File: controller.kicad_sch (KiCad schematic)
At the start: 24 parts, among them U1 nRF52840, X1 32MHz, X2 32.768kHz

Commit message: Start routing antennna
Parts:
- AE1: footprint (none) -> RF_Antenna:Texas_SWRA117D_2.4GHz_Left
- L1: footprint Inductor_SMD:L_6.3x6.3_H3 -> Inductor_SMD:L_0603_1608Metric
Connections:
- net VDD: now also C10.1, C5.1, C7.1, C8.1, C9.1, U1.A22 (VDD), U1.AD14 (VDD), U1.AD23 (VDD), U1.B1 (VDD), U1.W1 (VDD)
- net VDD_HV renamed VDDH
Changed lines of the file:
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@@
   (junction (at 72.39 113.03) (diameter 0) (color 0 0 0 0)
   )
-  (junction (at 50.8 27.94) (diameter 0) (color 0 0 0 0)
-  )
   (junction (at 149.86 36.83) (diameter 0) (color 0 0 0 0)
   )
@@
   (junction (at 72.39 123.19) (diameter 0) (color 0 0 0 0)
   )
-  (junction (at 140.97 16.51) (diameter 0) (color 0 0 0 0)
-  )
   (junction (at 72.39 57.15) (diameter 0) (color 0 0 0 0)
   )
@@
     (stroke (width 0) (type default))
   )
-  (wire (pts (xy 140.97 15.24) (xy 140.97 16.51))
-    (stroke (width 0) (type default))
-  )
   (wire (pts (xy 59.69 45.72) (xy 59.69 46.99))
     (stroke (width 0) (type default))
@@
     (stroke (width 0) (type default))
   )
-  (wire (pts (xy 41.91 27.94) (xy 50.8 27.94))
-    (stroke (width 0) (type default))
-  )
   (wire (pts (xy 46.99 44.45) (xy 46.99 46.99))
     (stroke (width 0) (type default))
@@
   (wire (pts (xy 72.39 121.92) (xy 72.39 123.19))
     (stroke (width 0) (type default))
-  )
-  (label "VDD_HV" (at 140.97 15.24 0) (fields_autoplaced)
-    (effects (font (size 1.27 1.27)) (justify left bottom))
   )
   (global_label "SWC" (shape input) (at 78.74 163.83 180) (fields_autoplaced)
@@
     )
   )
+  (global_label "VDDH" (shape input) (at 140.97 16.51 0) (fields_autoplaced)
+    (effects (font (size 1.27 1.27)) (justify left))
+    (property "Intersheetrefs" "${INTERSHEET_REFS}" (at 148.9143 16.51 0)
+      (effects (font (size 1.27 1.27)) (justify left) hide)
+    )
+  )
   (global_label "ROW4" (shape input) (at 144.78 69.85 0) (fields_autoplaced)
     (effects (font (size 1.27 1.27)) (justify left))
@@
     )
   )
+  (global_label "VDD" (shape input) (at 50.8 27.94 180) (fields_autoplaced)
+    (effects (font (size 1.27 1.27)) (justify right))
+    (property "Intersheetrefs" "${INTERSHEET_REFS}" (at 44.1862 27.94 0)
+      (effects (font (size 1.27 1.27)) (justify right) hide)
+    )
+  )
   (global_label "ROW1" (shape input) (at 144.78 146.05 0) (fields_autoplaced)
     (effects (font (size 1.27 1.27)) (justify left))
@@
       (effects (font (size 1.27 1.27)))
     )
-    (property "Footprint" "" (at 25.4 72.39 0)
+    (property "Footprint" "RF_Antenna:Texas_SWRA117D_2.4GHz_Left" (at 25.4 72.39 0)
       (effects (font (size 1.27 1.27)) hide)
     )
@@
       (effects (font (size 1.27 1.27)))
     )
-    (property "Footprint" "Inductor_SMD:L_6.3x6.3_H3" (at 128.27 45.72 0)
-      (effects (font (size 1.27 1.27)) hide)
-    )
+    (property "Footprint" "Inductor_SMD:L_0603_1608Metric" (at 128.27 45.72 0)
+      (effects (font (size 1.27 1.27)) hide)
+    )

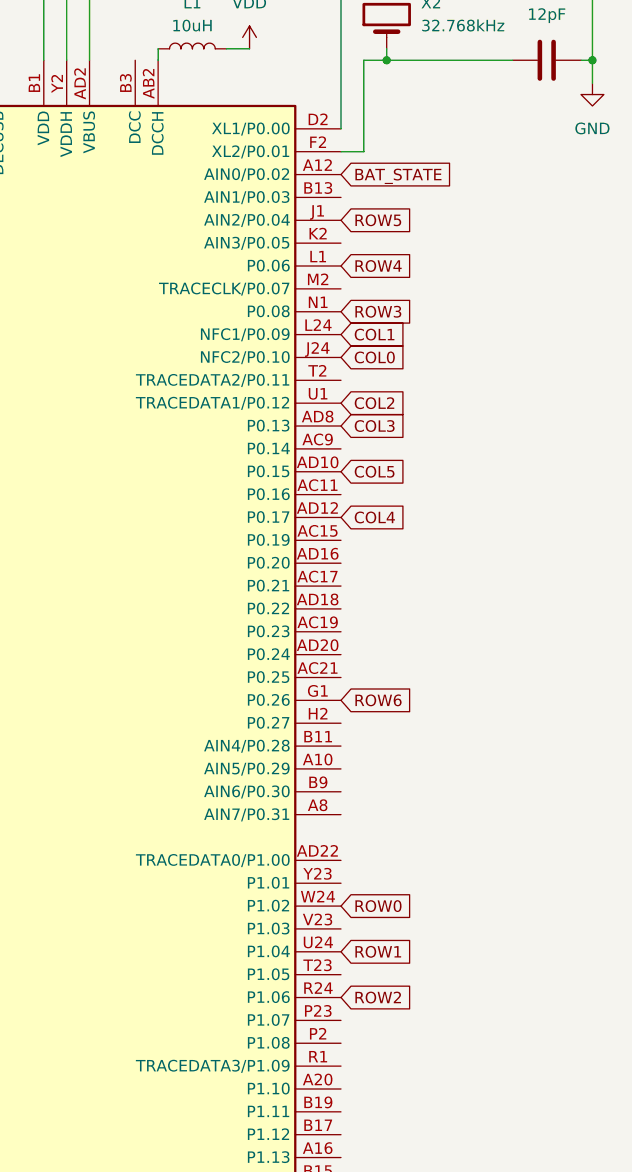
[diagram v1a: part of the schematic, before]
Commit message: Change board shape
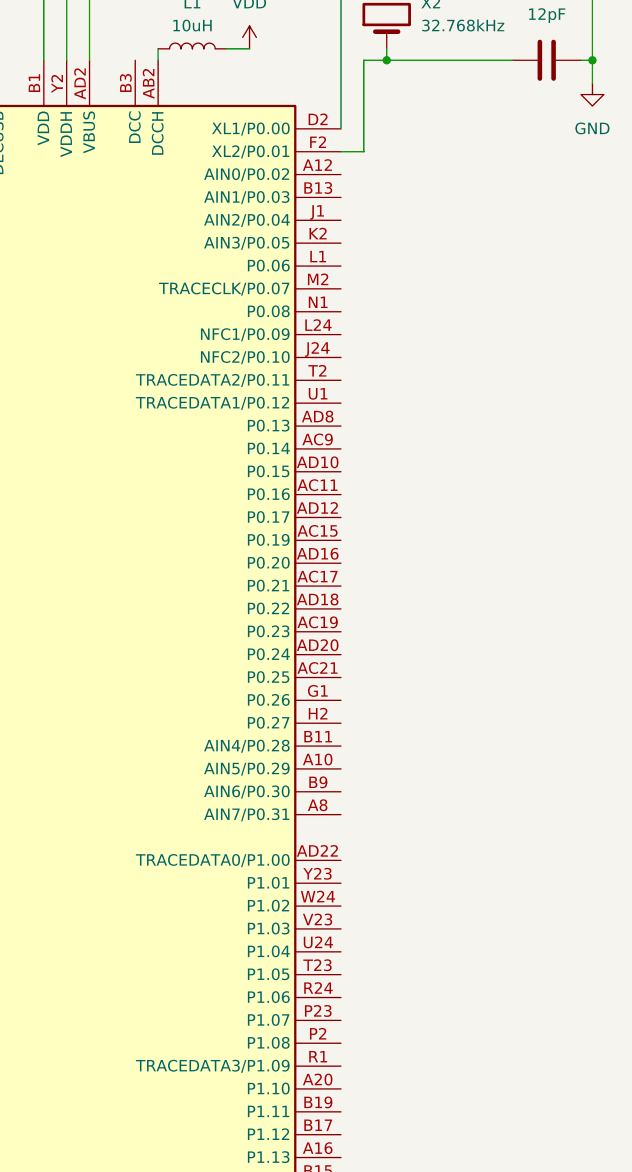
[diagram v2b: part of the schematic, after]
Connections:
- net BAT_STATE: no longer names the net of U1.A12 (AIN0/P0.02)
- net COL0: no longer names the net of U1.J24 (NFC2/P0.10)
- net COL1: no longer names the net of U1.L24 (NFC1/P0.09)
- net COL2: no longer names the net of U1.U1 (TRACEDATA1/P0.12)
- net COL3: no longer names the net of U1.AD8 (P0.13)
- net COL4: no longer names the net of U1.AD12 (P0.17)
- net COL5: no longer names the net of U1.AD10 (P0.15)
- net ROW0: no longer names the net of U1.W24 (P1.02)
- net ROW1: no longer names the net of U1.U24 (P1.04)
- net ROW2: no longer names the net of U1.R24 (P1.06)
- net ROW3: no longer names the net of U1.N1 (P0.08)
- net ROW4: no longer names the net of U1.L1 (P0.06)
- net ROW5: no longer names the net of U1.J1 (AIN2/P0.04)
- net ROW6: no longer names the net of U1.G1 (P0.26)
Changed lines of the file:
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@@
-    )
-  )
-  (global_label "ROW4" (shape input) (at 144.78 69.85 0) (fields_autoplaced)
-    (effects (font (size 1.27 1.27)) (justify left))
-    (property "Intersheetrefs" "${INTERSHEET_REFS}" (at 153.0266 69.85 0)
-      (effects (font (size 1.27 1.27)) (justify left) hide)
-    )
-  )
-  (global_label "ROW6" (shape input) (at 144.78 118.11 0) (fields_autoplaced)
-    (effects (font (size 1.27 1.27)) (justify left))
-    (property "Intersheetrefs" "${INTERSHEET_REFS}" (at 153.0266 118.11 0)
-      (effects (font (size 1.27 1.27)) (justify left) hide)
-    )
-  )
-  (global_label "BAT_STATE" (shape input) (at 144.78 59.69 0) (fields_autoplaced)
-    (effects (font (size 1.27 1.27)) (justify left))
-    (property "Intersheetrefs" "${INTERSHEET_REFS}" (at 157.4413 59.69 0)
-      (effects (font (size 1.27 1.27)) (justify left) hide)
-    )
-  )
-  (global_label "COL2" (shape input) (at 144.78 85.09 0) (fields_autoplaced)
-    (effects (font (size 1.27 1.27)) (justify left))
-    (property "Intersheetrefs" "${INTERSHEET_REFS}" (at 152.6033 85.09 0)
-      (effects (font (size 1.27 1.27)) (justify left) hide)
-    )
-  )
-  (global_label "COL4" (shape input) (at 144.78 97.79 0) (fields_autoplaced)
-    (effects (font (size 1.27 1.27)) (justify left))
-    (property "Intersheetrefs" "${INTERSHEET_REFS}" (at 152.6033 97.79 0)
-      (effects (font (size 1.27 1.27)) (justify left) hide)
-    )
-  )
-  (global_label "ROW0" (shape input) (at 144.78 140.97 0) (fields_autoplaced)
-    (effects (font (size 1.27 1.27)) (justify left))
-    (property "Intersheetrefs" "${INTERSHEET_REFS}" (at 153.0266 140.97 0)
-      (effects (font (size 1.27 1.27)) (justify left) hide)
-    )
-  )
-  (global_label "COL0" (shape input) (at 144.78 80.01 0) (fields_autoplaced)
-    (effects (font (size 1.27 1.27)) (justify left))
-    (property "Intersheetrefs" "${INTERSHEET_REFS}" (at 152.6033 80.01 0)
-      (effects (font (size 1.27 1.27)) (justify left) hide)
     )
   )
@@
     )
   )
-  (global_label "COL1" (shape input) (at 144.78 77.47 0) (fields_autoplaced)
-    (effects (font (size 1.27 1.27)) (justify left))
-    (property "Intersheetrefs" "${INTERSHEET_REFS}" (at 152.6033 77.47 0)
-      (effects (font (size 1.27 1.27)) (justify left) hide)
-    )
-  )
-  (global_label "COL3" (shape input) (at 144.78 87.63 0) (fields_autoplaced)
-    (effects (font (size 1.27 1.27)) (justify left))
-    (property "Intersheetrefs" "${INTERSHEET_REFS}" (at 152.6033 87.63 0)
-      (effects (font (size 1.27 1.27)) (justify left) hide)
-    )
-  )
-  (global_label "ROW2" (shape input) (at 144.78 151.13 0) (fields_autoplaced)
-    (effects (font (size 1.27 1.27)) (justify left))
-    (property "Intersheetrefs" "${INTERSHEET_REFS}" (at 153.0266 151.13 0)
-      (effects (font (size 1.27 1.27)) (justify left) hide)
-    )
-  )
   (global_label "VDD" (shape input) (at 50.8 27.94 180) (fields_autoplaced)
     (effects (font (size 1.27 1.27)) (justify right))
     (property "Intersheetrefs" "${INTERSHEET_REFS}" (at 44.1862 27.94 0)
       (effects (font (size 1.27 1.27)) (justify right) hide)
-    )
-  )
-  (global_label "ROW1" (shape input) (at 144.78 146.05 0) (fields_autoplaced)
-    (effects (font (size 1.27 1.27)) (justify left))
-    (property "Intersheetrefs" "${INTERSHEET_REFS}" (at 153.0266 146.05 0)
-      (effects (font (size 1.27 1.27)) (justify left) hide)
-    )
-  )
-  (global_label "ROW3" (shape input) (at 144.78 74.93 0) (fields_autoplaced)
-    (effects (font (size 1.27 1.27)) (justify left))
-    (property "Intersheetrefs" "${INTERSHEET_REFS}" (at 153.0266 74.93 0)
-      (effects (font (size 1.27 1.27)) (justify left) hide)
     )
   )
@@
     )
   )
-  (global_label "ROW5" (shape input) (at 144.78 64.77 0) (fields_autoplaced)
-    (effects (font (size 1.27 1.27)) (justify left))
-    (property "Intersheetrefs" "${INTERSHEET_REFS}" (at 153.0266 64.77 0)
-      (effects (font (size 1.27 1.27)) (justify left) hide)
-    )
-  )
-  (global_label "COL5" (shape input) (at 144.78 92.71 0) (fields_autoplaced)
-    (effects (font (size 1.27 1.27)) (justify left))
-    (property "Intersheetrefs" "${INTERSHEET_REFS}" (at 152.6033 92.71 0)
-      (effects (font (size 1.27 1.27)) (justify left) hide)
-    )
-  )

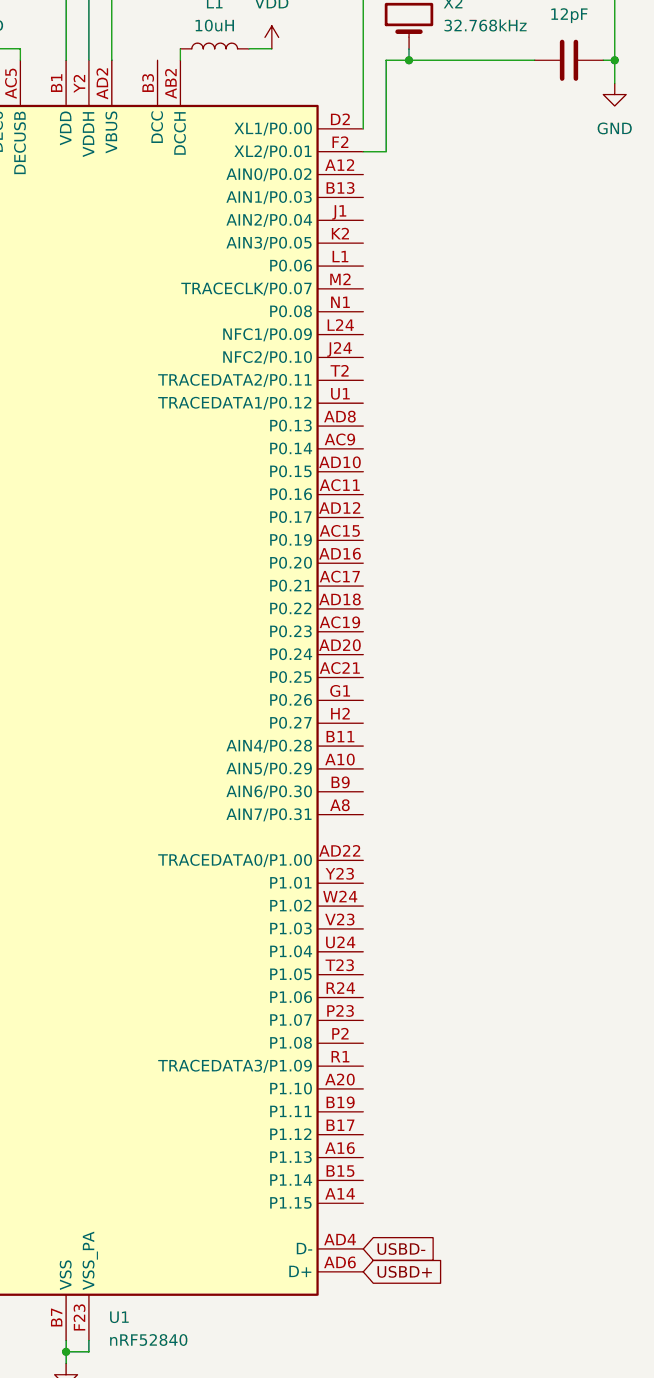
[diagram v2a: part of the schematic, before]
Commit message: Route rows and columns
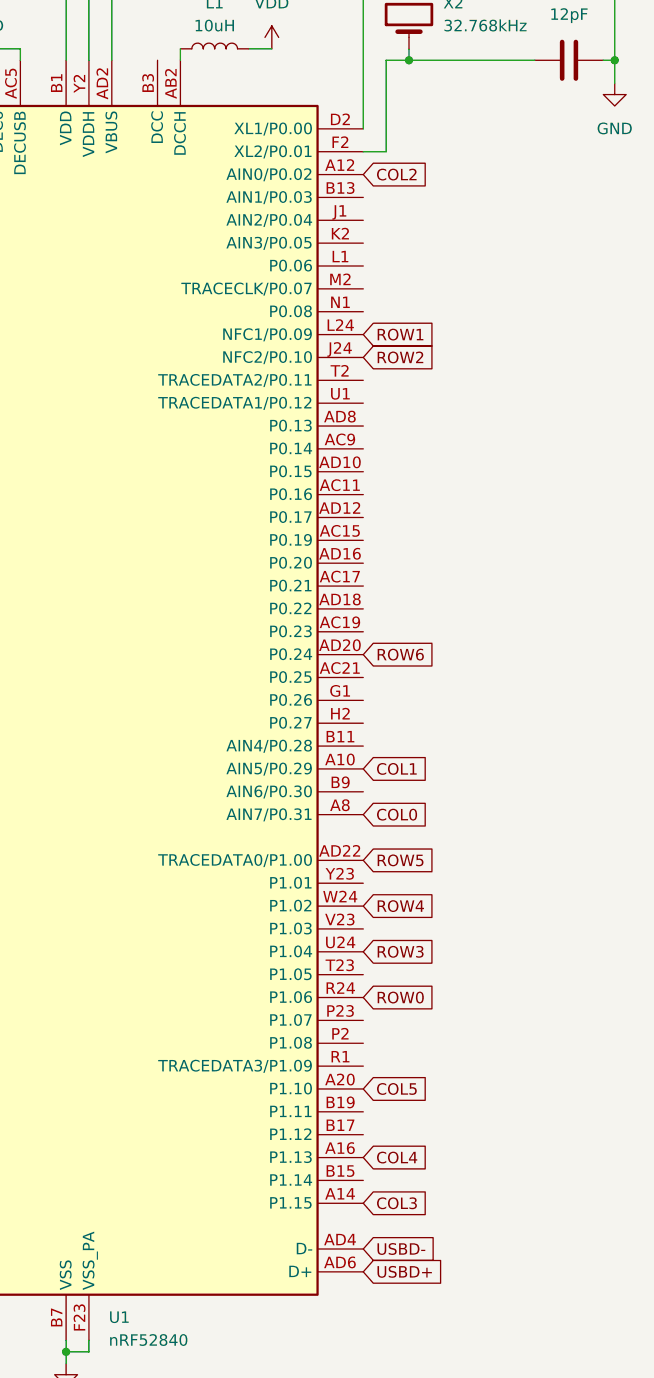
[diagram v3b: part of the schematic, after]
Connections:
- net COL1: now reaches U1.A10 (AIN5/P0.29)
- net COL2: now reaches U1.A12 (AIN0/P0.02)
- net COL3: now reaches U1.A14 (P1.15)
- net COL4: now reaches U1.A16 (P1.13)
- net COL5: now reaches U1.A20 (P1.10)
- net COL0: now reaches U1.A8 (AIN7/P0.31)
- net ROW6: now reaches U1.AD20 (P0.24)
- net ROW5: now reaches U1.AD22 (TRACEDATA0/P1.00)
- net ROW2: now reaches U1.J24 (NFC2/P0.10)
- net ROW1: now reaches U1.L24 (NFC1/P0.09)
- net ROW0: now reaches U1.R24 (P1.06)
- net ROW3: now reaches U1.U24 (P1.04)
- net ROW4: now reaches U1.W24 (P1.02)
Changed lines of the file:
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@@
+    )
+  )
+  (global_label "COL0" (shape input) (at 144.78 130.81 0) (fields_autoplaced)
+    (effects (font (size 1.27 1.27)) (justify left))
+    (property "Intersheetrefs" "${INTERSHEET_REFS}" (at 152.6033 130.81 0)
+      (effects (font (size 1.27 1.27)) (justify left) hide)
     )
   )
@@
     (effects (font (size 1.27 1.27)) (justify left))
     (property "Intersheetrefs" "${INTERSHEET_REFS}" (at 148.9143 16.51 0)
+      (effects (font (size 1.27 1.27)) (justify left) hide)
+    )
+  )
+  (global_label "ROW3" (shape input) (at 144.78 146.05 0) (fields_autoplaced)
+    (effects (font (size 1.27 1.27)) (justify left))
+    (property "Intersheetrefs" "${INTERSHEET_REFS}" (at 153.0266 146.05 0)
       (effects (font (size 1.27 1.27)) (justify left) hide)
     )
@@
     )
   )
+  (global_label "ROW4" (shape input) (at 144.78 140.97 0) (fields_autoplaced)
+    (effects (font (size 1.27 1.27)) (justify left))
+    (property "Intersheetrefs" "${INTERSHEET_REFS}" (at 153.0266 140.97 0)
+      (effects (font (size 1.27 1.27)) (justify left) hide)
+    )
+  )
+  (global_label "ROW0" (shape input) (at 144.78 151.13 0) (fields_autoplaced)
+    (effects (font (size 1.27 1.27)) (justify left))
+    (property "Intersheetrefs" "${INTERSHEET_REFS}" (at 153.0266 151.13 0)
+      (effects (font (size 1.27 1.27)) (justify left) hide)
+    )
+  )
+  (global_label "ROW6" (shape input) (at 144.78 113.03 0) (fields_autoplaced)
+    (effects (font (size 1.27 1.27)) (justify left))
+    (property "Intersheetrefs" "${INTERSHEET_REFS}" (at 153.0266 113.03 0)
+      (effects (font (size 1.27 1.27)) (justify left) hide)
+    )
+  )
+  (global_label "ROW1" (shape input) (at 144.78 77.47 0) (fields_autoplaced)
+    (effects (font (size 1.27 1.27)) (justify left))
+    (property "Intersheetrefs" "${INTERSHEET_REFS}" (at 153.0266 77.47 0)
+      (effects (font (size 1.27 1.27)) (justify left) hide)
+    )
+  )
+  (global_label "COL3" (shape input) (at 144.78 173.99 0) (fields_autoplaced)
+    (effects (font (size 1.27 1.27)) (justify left))
+    (property "Intersheetrefs" "${INTERSHEET_REFS}" (at 152.6033 173.99 0)
+      (effects (font (size 1.27 1.27)) (justify left) hide)
+    )
+  )
+  (global_label "COL2" (shape input) (at 144.78 59.69 0) (fields_autoplaced)
+    (effects (font (size 1.27 1.27)) (justify left))
+    (property "Intersheetrefs" "${INTERSHEET_REFS}" (at 152.6033 59.69 0)
+      (effects (font (size 1.27 1.27)) (justify left) hide)
+    )
+  )
+  (global_label "COL5" (shape input) (at 144.78 161.29 0) (fields_autoplaced)
+    (effects (font (size 1.27 1.27)) (justify left))
+    (property "Intersheetrefs" "${INTERSHEET_REFS}" (at 152.6033 161.29 0)
+      (effects (font (size 1.27 1.27)) (justify left) hide)
+    )
+  )
+  (global_label "ROW2" (shape input) (at 144.78 80.01 0) (fields_autoplaced)
+    (effects (font (size 1.27 1.27)) (justify left))
+    (property "Intersheetrefs" "${INTERSHEET_REFS}" (at 153.0266 80.01 0)
+      (effects (font (size 1.27 1.27)) (justify left) hide)
+    )
+  )
   (global_label "VDD" (shape input) (at 50.8 27.94 180) (fields_autoplaced)
     (effects (font (size 1.27 1.27)) (justify right))
     (property "Intersheetrefs" "${INTERSHEET_REFS}" (at 44.1862 27.94 0)
       (effects (font (size 1.27 1.27)) (justify right) hide)
+    )
+  )
+  (global_label "COL4" (shape input) (at 144.78 168.91 0) (fields_autoplaced)
+    (effects (font (size 1.27 1.27)) (justify left))
+    (property "Intersheetrefs" "${INTERSHEET_REFS}" (at 152.6033 168.91 0)
+      (effects (font (size 1.27 1.27)) (justify left) hide)
     )
   )
@@
     )
   )
+  (global_label "ROW5" (shape input) (at 144.78 135.89 0) (fields_autoplaced)
+    (effects (font (size 1.27 1.27)) (justify left))
+    (property "Intersheetrefs" "${INTERSHEET_REFS}" (at 153.0266 135.89 0)
+      (effects (font (size 1.27 1.27)) (justify left) hide)
+    )
+  )
+  (global_label "COL1" (shape input) (at 144.78 125.73 0) (fields_autoplaced)
+    (effects (font (size 1.27 1.27)) (justify left))
+    (property "Intersheetrefs" "${INTERSHEET_REFS}" (at 152.6033 125.73 0)
+      (effects (font (size 1.27 1.27)) (justify left) hide)
+    )
+  )
